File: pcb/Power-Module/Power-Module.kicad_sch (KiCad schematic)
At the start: 1 part

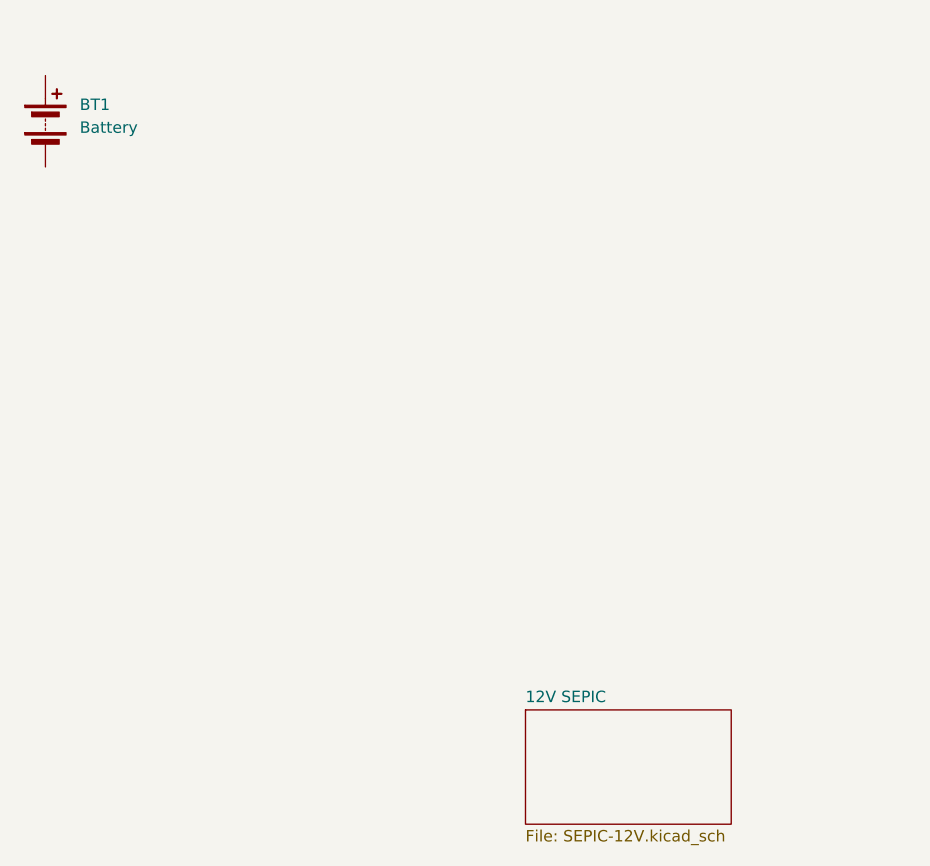
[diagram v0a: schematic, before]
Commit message: Created system-level hierarch. Implemented 3.3V buck converter based on TI WEBBENCH Power Designer.
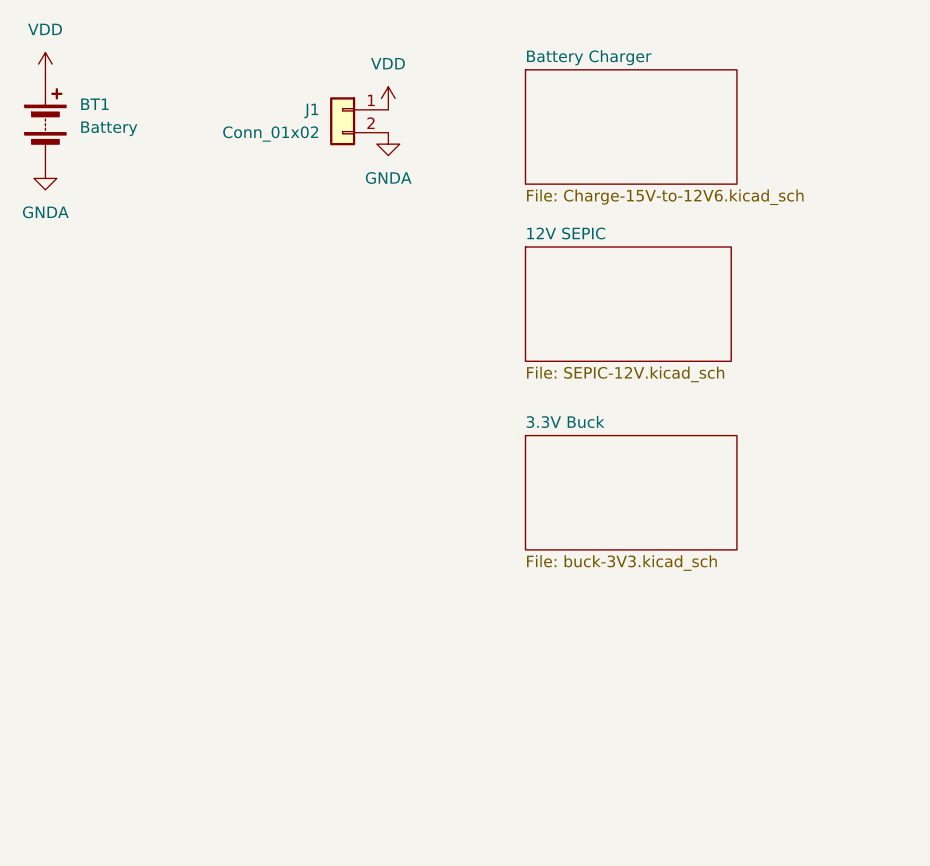
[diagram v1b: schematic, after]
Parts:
- added J1: Conn_01x02, symbol Connector_Generic:Conn_01x02
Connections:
- net VDD: now reaches BT1.1 (+)
- net VDD: now also J1.1 (Pin_1)
- net GNDA: now reaches BT1.2 (-)
- net GNDA: now also J1.2 (Pin_2)
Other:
- added sheet 3.3V Buck (buck-3V3.kicad_sch)
- added sheet Battery Charger (Charge-15V-to-12V6.kicad_sch)
